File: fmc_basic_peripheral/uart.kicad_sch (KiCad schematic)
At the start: 27 parts, among them J3 USB_C_Receptacle, U12 TPD4E02B04DQA, U14 TXS02612RTWR, U3 CP2104

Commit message: uart.kicad_sch: replace cp2104 with ch9102f
After testing, cp2104 is unstable at the moment of power-on,
so it is replaced with ch9102f to fix this issue.

Signed-off-by: Huang Rui <vowstar@gmail.com>
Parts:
- U3: value CP2104 -> CH9102F; footprint Package_DFN_QFN:QFN-24-1EP_4x4mm_P0.5mm_EP2.6x2.6mm -> CHIPSAlliance_Package_DFN_QFN:QFN-24-1EP_4x4mm_P0.5mm_EP2.6x2.6mm; symbol CHIPSAlliance_Interface:CP2104 -> CHIPSAlliance_Interface:CH9102F
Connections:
- no-connect marks 23 -> 24
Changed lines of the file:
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@@
   (no_connect (at 63.5 116.84))
   (no_connect (at 245.11 129.54))
+  (no_connect (at 170.18 81.28))
   (no_connect (at 33.02 96.52))
   (no_connect (at 63.5 106.68))
@@
     )
   )
-  (symbol (lib_id "CHIPSAlliance_Interface:CP2104") (at 193.04 76.2 0) (mirror y) (unit 1)
+  (symbol (lib_id "CHIPSAlliance_Interface:CH9102F") (at 193.04 76.2 0) (mirror y) (unit 1)
     (in_bom yes) (on_board yes) (dnp no)
     (property "Reference" "U3" (at 175.26 74.93 0)
       (effects (font (size 1.27 1.27)) (justify left))
     )
-    (property "Value" "CP2104" (at 193.04 74.93 0)
+    (property "Value" "CH9102F" (at 193.04 128.27 0)
       (effects (font (size 1.27 1.27)) (justify left))
     )
-    (property "Footprint" "Package_DFN_QFN:QFN-24-1EP_4x4mm_P0.5mm_EP2.6x2.6mm" (at 193.04 130.81 0)
+    (property "Footprint" "CHIPSAlliance_Package_DFN_QFN:QFN-24-1EP_4x4mm_P0.5mm_EP2.6x2.6mm" (at 193.04 130.81 0)
       (effects (font (size 1.27 1.27)) (justify left) hide)
     )
-    (property "Datasheet" "https://www.silabs.com/documents/public/data-sheets/cp2104.pdf" (at 193.04 133.35 0)
+    (property "Datasheet" "https://atta.szlcsc.com/upload/public/pdf/source/20211016/C2858418_C3D66D242DBFEF06B4830254B68CDF56.pdf" (at 193.04 133.35 0)
       (effects (font (size 1.27 1.27)) (justify left) hide)
     )

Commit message: *.kicad_sch: update footprint for QFN*
Signed-off-by: Huang Rui <vowstar@gmail.com>
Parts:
- U14: footprint CHIPSAlliance_Logic:WQFN-24-1EP_4x4mm_P0.5mm_EP2.45x2.45mm -> CHIPSAlliance_Package_DFN_QFN:WQFN-24-1EP_4x4mm_P0.5mm_EP2.45x2.45mm
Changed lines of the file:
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@@
       (effects (font (size 1.27 1.27)) (justify left))
     )
-    (property "Footprint" "CHIPSAlliance_Logic:WQFN-24-1EP_4x4mm_P0.5mm_EP2.45x2.45mm" (at 35.56 127 0)
+    (property "Footprint" "CHIPSAlliance_Package_DFN_QFN:WQFN-24-1EP_4x4mm_P0.5mm_EP2.45x2.45mm" (at 35.56 127 0)
       (effects (font (size 1.27 1.27)) (justify left) hide)
     )

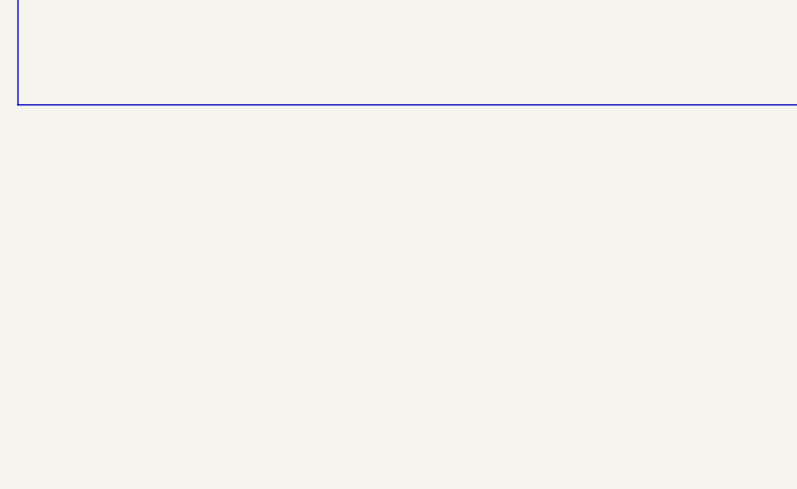
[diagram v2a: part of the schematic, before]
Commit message: uart.kicad_sch: add annotation for FMC UART crossing
Signed-off-by: Huang Rui <vowstar@gmail.com>
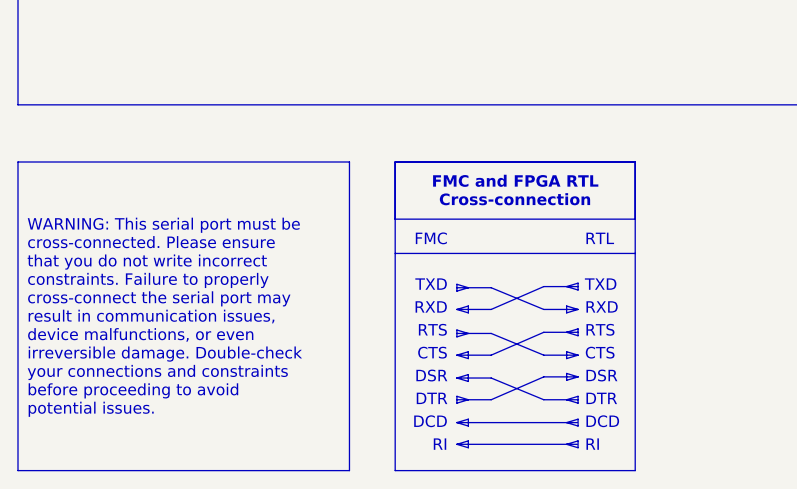
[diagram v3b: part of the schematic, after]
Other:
- note added: "CTS"
- note added: "DCD"
- note added: "DSR"
- note added: "DTR"
- note added: "FMC"
- note added: "RI"
- note added: "RTL"
- note added: "RTS"
- note added: "RXD"
- note added: "TXD"

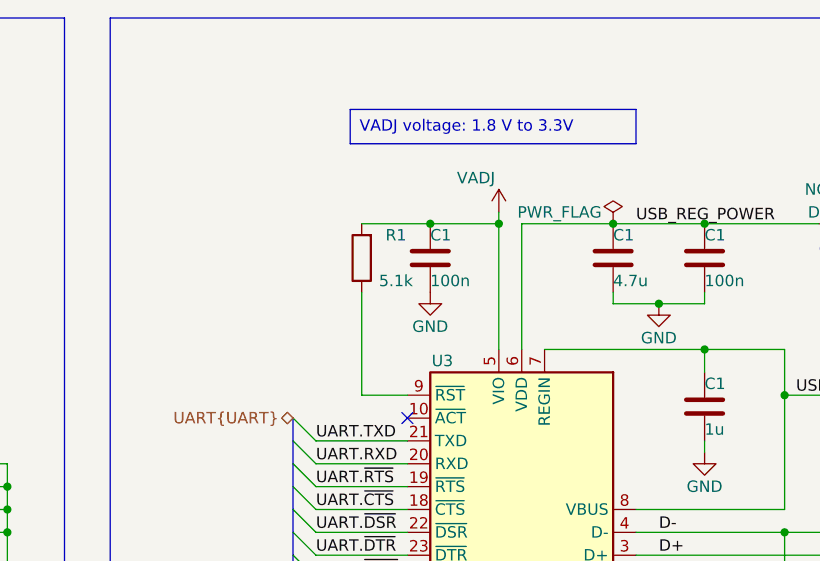
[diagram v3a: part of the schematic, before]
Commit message: uart.kicad_sch: add ~{SRST} to CH9102F
- Fix bugs and enhance error handling in the UART module

Signed-off-by: Huang Rui <vowstar@gmail.com>
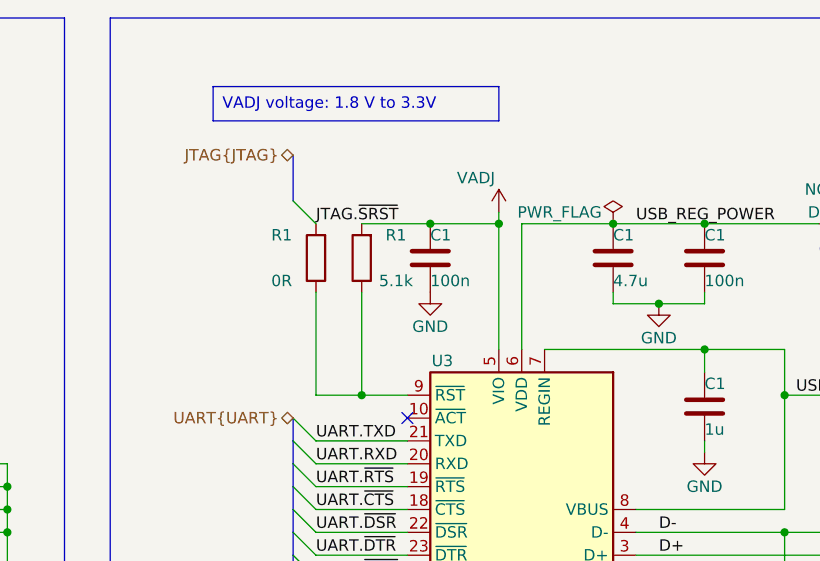
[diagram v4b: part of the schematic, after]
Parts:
- added R1: 0R, Resistor_SMD:R_0402_1005Metric, symbol Device:R
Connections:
- net at R1.1, U3.9 (~{RST}): now also R1.1
- new net JTAG.~{SRST}: R1.2

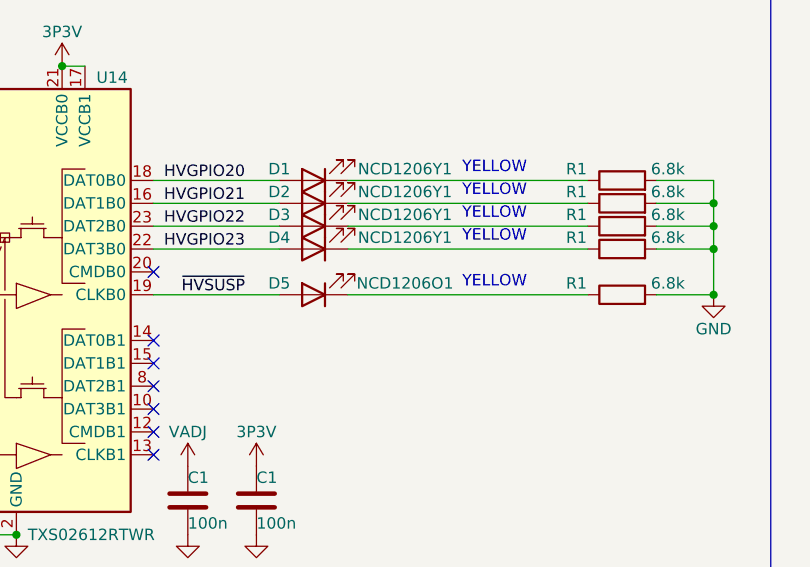
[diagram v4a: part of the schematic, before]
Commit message: uart.kicad_sch: change D5 to NCD1206Y1
- fix color of D5

Signed-off-by: Huang Rui <vowstar@gmail.com>
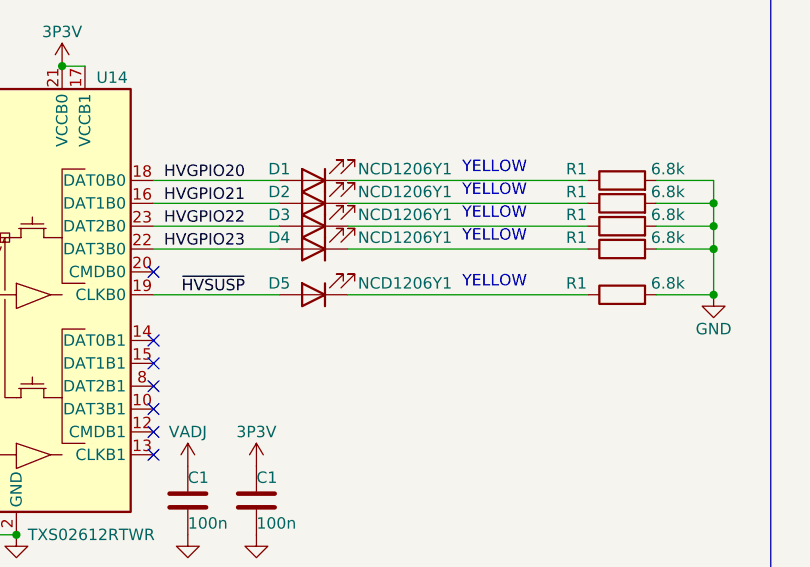
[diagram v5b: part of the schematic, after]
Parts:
- D5: value NCD1206O1 -> NCD1206Y1
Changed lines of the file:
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@@
       (effects (font (size 1.27 1.27)))
     )
-    (property "Value" "NCD1206O1" (at 91.44 97.79 0)
+    (property "Value" "NCD1206Y1" (at 91.44 97.79 0)
       (effects (font (size 1.27 1.27)))
     )
